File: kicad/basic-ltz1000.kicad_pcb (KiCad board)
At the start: 2 copper layers, 49.5 x 49.5 mm, 43 parts, among them P1 CONN_1X1, P2 CONN_1X1, P3 CONN_1X1, P4 CONN_1X1, P5 CONN_1X1, P6 CONN_2X1, Q1 2N3904, U1 LTZ1000A, U2 LT1013, U30 LTC2057

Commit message: 2.3
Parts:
- added R45: 13k/1k, R_BOX_DIVIDER_PL, F.Cu at (205.1, 93.3)
- moved R4 3.42 mm to (204.5, 96.5)
- moved R5 3.42 mm to (202.6, 98.4)
- moved R2 1.27 mm to (205.1, 71.8)
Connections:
- U30 pad 1: 15V -> (no net)
- U30 pad 8: Vz- Sense -> (no net)
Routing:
- net N-000008: track 26.1 -> 32.7 mm
- net 15V: track 60.1 -> 54.0 mm
- net Vz- Sense: track 245.9 -> 240.1 mm, vias 3 -> 2
- net Vz+ Sense: track 125.0 -> 129.3 mm
- net N-0000023: track 55.3 -> 57.8 mm
- net N-0000014: track 52.9 -> 53.5 mm
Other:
- board text added: "v2.3"
- board text removed: "v2.2b"

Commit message: v2.4 gerbers
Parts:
- removed the G*** at (201.3, 67.7)
- removed P6: CONN_2X1, SIL-2
- added G***: OSHW-logo_silkscreen-front_3mm, OSHW-logo_silkscreen-front_3mm, F.Cu at (200.5, 69.5)
- added H***: Val**, 1pin_032_058, F.Cu at (246.0, 85.9)
- added H***: Val**, 1pin_032_058, F.Cu at (246.0, 91.9)
- added H***: Val**, 1pin_032_058, F.Cu at (199.4, 101.6)
- moved R19 3.14 mm to (213.9, 106.8), turned to 160 degrees
- moved H*** 2.62 mm to (242.6, 71.8)
- moved C30 1.91 mm to (241.9, 80.6)
- moved C31 1.91 mm to (241.9, 83.2)
- moved R31 1.42 mm to (245.7, 77.5)
- moved U30 1.27 mm to (242.6, 88.9)
- moved C33 1.27 mm to (242.6, 94.6)
- moved P1 1.27 mm to (210.8, 111.8)
- moved P4 1.27 mm to (208.3, 111.8)
- moved R2 0.90 mm to (205.7, 72.4)
- moved H1 0.64 mm to (202.6, 109.2)
- moved P2 0.64 mm to (217.8, 69.2)
- moved P3 0.64 mm to (236.2, 92.1)
- moved R32 0.64 mm to (236.2, 79.4)
- moved D3 0.63 mm to (236.9, 111.8)
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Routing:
- net Vz- Sense: track 240.1 -> 220.2 mm
- net (no net): track 0.00 -> 7.94 mm
- net CHASSIS: track 6.54 -> 0.00 mm
- net N-000007: track 14.4 -> 17.1 mm
- net 15V: track 54.0 -> 51.6 mm
- net Vz+ Sense: track 129.3 -> 127.0 mm
- net N-0000023: track 57.8 -> 55.5 mm
- net N-0000012: track 14.2 -> 15.8 mm
- net Vz+ Buf: track 16.2 -> 15.3 mm
- net N-0000014: track 53.5 -> 52.7 mm
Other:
- board size 49.5 x 49.5 mm -> 48.9 x 46.4 mm
- board text added: "+ SD -"
- board text added: "TSET"
- board text added: "v2.4"
- board text removed: "CHASSIS"
- board text removed: "v2.3"

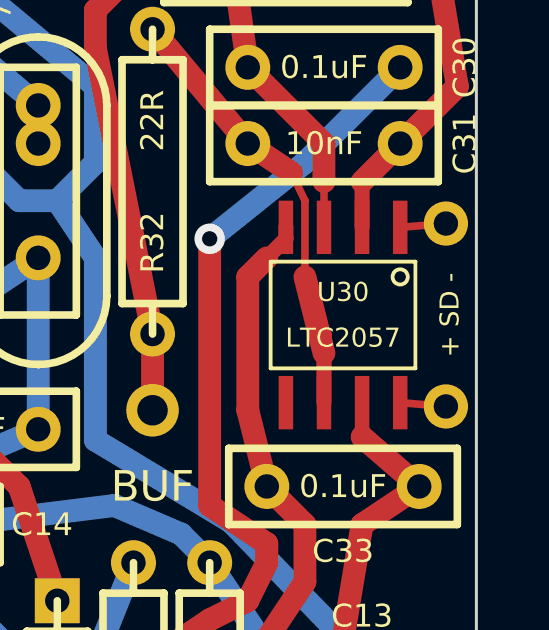
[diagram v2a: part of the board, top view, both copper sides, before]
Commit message: silkscreen typo
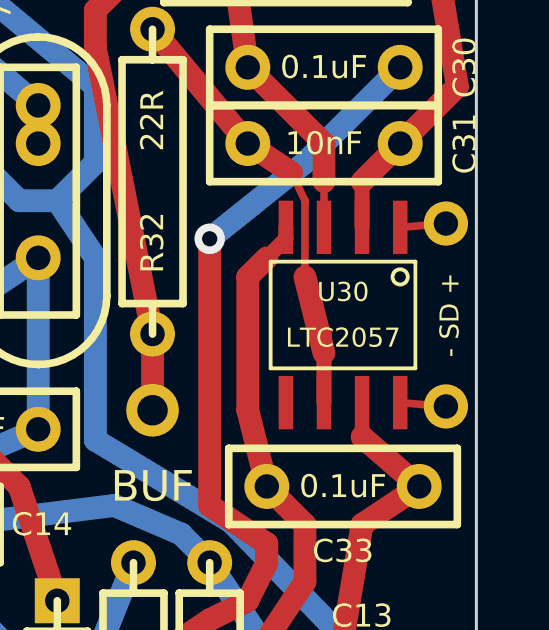
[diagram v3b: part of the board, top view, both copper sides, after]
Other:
- board text added: "- SD +"
- board text removed: "+ SD -"
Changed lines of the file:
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@@
     (links 76)
     (no_connects 0)
-    (area 196.1388 64.388999 248.031001 116.459)
+    (area 196.186778 65.786 249.202222 115.189)
     (thickness 1.6)
     (drawings 21)
@@
     )
   )
-  (gr_text "+ SD -" (at 246.126 88.9 90) (layer F.SilkS)
+  (gr_text "- SD +" (at 246.126 88.9 90) (layer F.SilkS)
     (effects (font (size 0.635 0.635) (thickness 0.127)))
   )

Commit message: v2.4.1
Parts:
- added C32: 0.1uF, BOXCAP_01_03_02_059A, F.Cu at (229.9, 90.2)
- added C9: 0.1uF, BOXCAP_01_03_02_059A, F.Cu at (211.5, 108.6)
- moved D1 8.25 mm to (228.6, 82.5), turned to 270 degrees
- moved R19 3.30 mm to (214.0, 103.5), turned to 180 degrees
- moved R3 2.54 mm to (232.4, 82.5)
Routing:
- net Vz- Sense: track 220.2 -> 240.3 mm
- net N-000005: track 18.6 -> 11.3 mm
- net N-0000023: track 32.3 -> 36.9 mm
- net N-000007: track 8.89 -> 13.4 mm
- net Vz+ Buf: track 15.3 -> 19.6 mm
- net N-000001: track 17.1 -> 19.6 mm
- net Vz+ Sense: track 127.0 -> 127.8 mm
- net H+: track 66.6 -> 67.3 mm
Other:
- board text added: "T SET"
- board text added: "v2.4.1"
- board text removed: "TSET"
- board text removed: "v2.4"

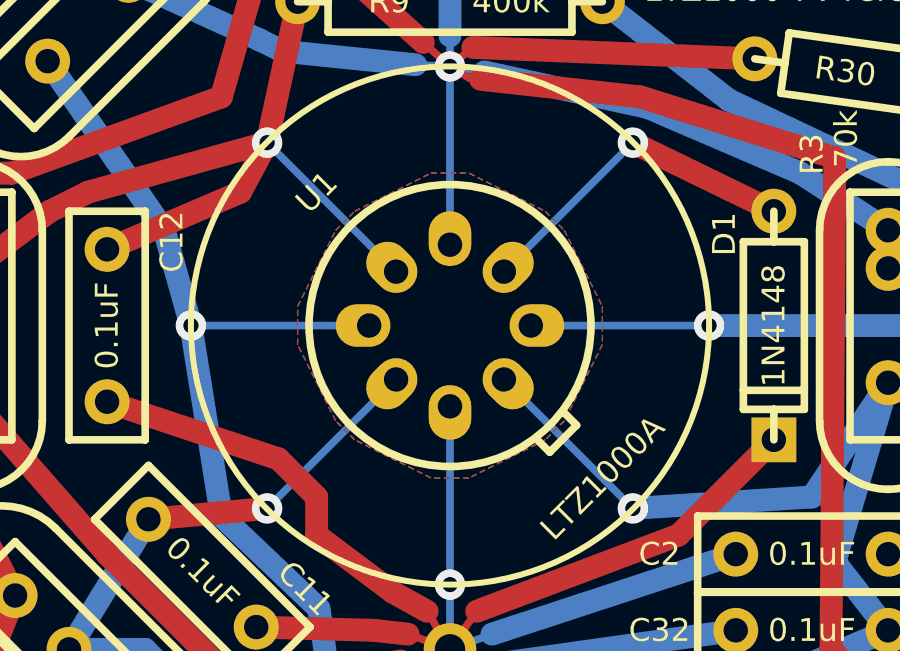
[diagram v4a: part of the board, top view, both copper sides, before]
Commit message: adding vias
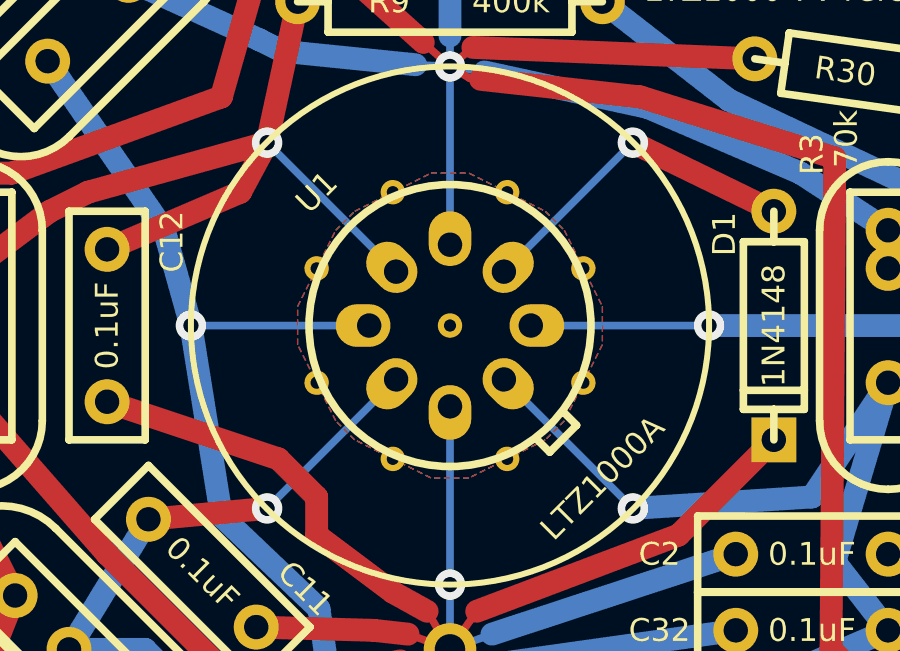
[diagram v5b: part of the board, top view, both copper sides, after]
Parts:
- added H***: Val**, Via_016, F.Cu at (215.9, 87.0)
- added H***: Val**, Via_016, F.Cu at (213.4, 84.5)
- added H***: Val**, Via_016, F.Cu at (213.4, 80.6)
- added H***: Val**, Via_016, F.Cu at (215.9, 78.1)
- added H***: Val**, Via_016, F.Cu at (217.8, 82.5)
- added H***: Val**, Via_016, F.Cu at (219.7, 78.1)
- added H***: Val**, Via_016, F.Cu at (222.2, 80.6)
- added H***: Val**, Via_016, F.Cu at (222.2, 84.5)
- added H***: Val**, Via_016, F.Cu at (219.7, 87.0)
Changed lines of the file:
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@@
     (tracks 267)
     (zones 0)
-    (modules 48)
+    (modules 57)
     (nets 23)
   )
@@
     )
   )
+  (module Via_016 (layer F.Cu)
+    (at 217.805 82.55)
+    (descr "Via, 0.016\"")
+    (path 1pin)
+    (fp_text reference H*** (at 0 -0.635) (layer F.SilkS) hide
+      (effects (font (size 0.127 0.127) (thickness 0.000001)))
+    )
+    (fp_text value Val** (at 0 0.635) (layer F.SilkS) hide
+      (effects (font (size 0.127 0.127) (thickness 0.000001)))
+    )
+    (pad ~ thru_hole oval (at 0 0) (size 0.8128 0.8128) (drill 0.4064)
+      (layers *.Cu)
+      (zone_connect 2)
+    )
+  )
+  (module Via_016 (layer F.Cu)
+    (at 219.71 78.105)
+    (descr "Via, 0.016\"")
+    (path 1pin)
+    (fp_text reference H*** (at 0 -0.635) (layer F.SilkS) hide
+      (effects (font (size 0.127 0.127) (thickness 0.000001)))
+    )
+    (fp_text value Val** (at 0 0.635) (layer F.SilkS) hide
+      (effects (font (size 0.127 0.127) (thickness 0.000001)))
+    )
+    (pad ~ thru_hole oval (at 0 0) (size 0.8128 0.8128) (drill 0.4064)
+      (layers *.Cu)
+      (zone_connect 2)
+    )
+  )
+  (module Via_016 (layer F.Cu)
+    (at 222.25 80.645)
+    (descr "Via, 0.016\"")
+    (path 1pin)
+    (fp_text reference H*** (at 0 -0.635) (layer F.SilkS) hide
+      (effects (font (size 0.127 0.127) (thickness 0.000001)))
+    )
+    (fp_text value Val** (at 0 0.635) (layer F.SilkS) hide
+      (effects (font (size 0.127 0.127) (thickness 0.000001)))
+    )
+    (pad ~ thru_hole oval (at 0 0) (size 0.8128 0.8128) (drill 0.4064)
+      (layers *.Cu)
+      (zone_connect 2)
+    )
+  )
+  (module Via_016 (layer F.Cu)
+    (at 222.25 84.455)
+    (descr "Via, 0.016\"")
+    (path 1pin)
+    (fp_text reference H*** (at 0 -0.635) (layer F.SilkS) hide
+      (effects (font (size 0.127 0.127) (thickness 0.000001)))
+    )
+    (fp_text value Val** (at 0 0.635) (layer F.SilkS) hide
+      (effects (font (size 0.127 0.127) (thickness 0.000001)))
+    )
+    (pad ~ thru_hole oval (at 0 0) (size 0.8128 0.8128) (drill 0.4064)
+      (layers *.Cu)
+      (zone_connect 2)
+    )
+  )
+  (module Via_016 (layer F.Cu)
+    (at 219.71 86.995)
+    (descr "Via, 0.016\"")
+    (path 1pin)
+    (fp_text reference H*** (at 0 -0.635) (layer F.SilkS) hide
+      (effects (font (size 0.127 0.127) (thickness 0.000001)))
+    )
+    (fp_text value Val** (at 0 0.635) (layer F.SilkS) hide
+      (effects (font (size 0.127 0.127) (thickness 0.000001)))
+    )
+    (pad ~ thru_hole oval (at 0 0) (size 0.8128 0.8128) (drill 0.4064)
+      (layers *.Cu)
+      (zone_connect 2)
+    )
+  )
+  (module Via_016 (layer F.Cu)
+    (at 215.9 86.995)
+    (descr "Via, 0.016\"")
+    (path 1pin)
+    (fp_text reference H*** (at 0 -0.635) (layer F.SilkS) hide
+      (effects (font (size 0.127 0.127) (thickness 0.000001)))
+    )
+    (fp_text value Val** (at 0 0.635) (layer F.SilkS) hide
+      (effects (font (size 0.127 0.127) (thickness 0.000001)))
+    )
+    (pad ~ thru_hole oval (at 0 0) (size 0.8128 0.8128) (drill 0.4064)
+      (layers *.Cu)
+      (zone_connect 2)
+    )
+  )
+  (module Via_016 (layer F.Cu)
+    (at 213.36 84.455)
+    (descr "Via, 0.016\"")
+    (path 1pin)
+    (fp_text reference H*** (at 0 -0.635) (layer F.SilkS) hide
+      (effects (font (size 0.127 0.127) (thickness 0.000001)))
+    )
+    (fp_text value Val** (at 0 0.635) (layer F.SilkS) hide
+      (effects (font (size 0.127 0.127) (thickness 0.000001)))
+    )
+    (pad ~ thru_hole oval (at 0 0) (size 0.8128 0.8128) (drill 0.4064)
+      (layers *.Cu)
+      (zone_connect 2)
+    )
+  )
+  (module Via_016 (layer F.Cu)
+    (at 213.36 80.645)
+    (descr "Via, 0.016\"")
+    (path 1pin)
+    (fp_text reference H*** (at 0 -0.635) (layer F.SilkS) hide
+      (effects (font (size 0.127 0.127) (thickness 0.000001)))
+    )
+    (fp_text value Val** (at 0 0.635) (layer F.SilkS) hide
+      (effects (font (size 0.127 0.127) (thickness 0.000001)))
+    )
+    (pad ~ thru_hole oval (at 0 0) (size 0.8128 0.8128) (drill 0.4064)
+      (layers *.Cu)
+      (zone_connect 2)
+    )
+  )
+  (module Via_016 (layer F.Cu)
+    (at 215.9 78.105)
+    (descr "Via, 0.016\"")
+    (path 1pin)
+    (fp_text reference H*** (at 0 -0.635) (layer F.SilkS) hide
+      (effects (font (size 0.127 0.127) (thickness 0.000001)))
+    )
+    (fp_text value Val** (at 0 0.635) (layer F.SilkS) hide
+      (effects (font (size 0.127 0.127) (thickness 0.000001)))
+    )
+    (pad ~ thru_hole oval (at 0 0) (size 0.8128 0.8128) (drill 0.4064)
+      (layers *.Cu)
+      (zone_connect 2)
+    )
+  )

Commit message: v2.4.2
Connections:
- H*** pad ~: (no net) -> CHASSIS (x9)
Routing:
- added copper zone on B.Cu, net CHASSIS
- added copper zone on F.Cu, net CHASSIS
- removed copper zone on B.Cu, net (none)
- removed copper zone on F.Cu, net (none)
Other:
- board text added: "v2.4.2"
- board text removed: "v2.4.1"
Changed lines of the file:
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@@
 (kicad_pcb (version 3) (host pcbnew "(22-Jun-2014 BZR 4027)-stable")
   (general
-    (links 80)
-    (no_connects 0)
+    (links 89)
+    (no_connects 2)
     (area 196.186778 65.786 249.202222 115.189)
     (thickness 1.6)
@@
     (mod_text_size 1 1)
     (mod_text_width 0.15)
-    (pad_size 8.255 8.255)
-    (pad_drill 3.2)
+    (pad_size 0.8128 0.8128)
+    (pad_drill 0.4064)
     (pad_to_mask_clearance 0)
     (aux_axis_origin 0 0)
@@
     (pad ~ thru_hole oval (at 0 0) (size 0.8128 0.8128) (drill 0.4064)
       (layers *.Cu)
+      (net 2 CHASSIS)
       (zone_connect 2)
     )
@@
     (pad ~ thru_hole oval (at 0 0) (size 0.8128 0.8128) (drill 0.4064)
       (layers *.Cu)
+      (net 2 CHASSIS)
       (zone_connect 2)
     )
@@
     (pad ~ thru_hole oval (at 0 0) (size 0.8128 0.8128) (drill 0.4064)
       (layers *.Cu)
+      (net 2 CHASSIS)
       (zone_connect 2)
     )
@@
     (pad ~ thru_hole oval (at 0 0) (size 0.8128 0.8128) (drill 0.4064)
       (layers *.Cu)
+      (net 2 CHASSIS)
       (zone_connect 2)
     )
@@
     (pad ~ thru_hole oval (at 0 0) (size 0.8128 0.8128) (drill 0.4064)
       (layers *.Cu)
+      (net 2 CHASSIS)
       (zone_connect 2)
     )
@@
     (pad ~ thru_hole oval (at 0 0) (size 0.8128 0.8128) (drill 0.4064)
       (layers *.Cu)
+      (net 2 CHASSIS)
       (zone_connect 2)
     )
@@
     (pad ~ thru_hole oval (at 0 0) (size 0.8128 0.8128) (drill 0.4064)
       (layers *.Cu)
+      (net 2 CHASSIS)
       (zone_connect 2)
     )
@@
     (pad ~ thru_hole oval (at 0 0) (size 0.8128 0.8128) (drill 0.4064)
       (layers *.Cu)
+      (net 2 CHASSIS)
       (zone_connect 2)
     )
@@
     (pad ~ thru_hole oval (at 0 0) (size 0.8128 0.8128) (drill 0.4064)
       (layers *.Cu)
+      (net 2 CHASSIS)
       (zone_connect 2)
     )
@@
     (effects (font (size 0.762 0.762) (thickness 0.1524)) (justify left mirror))
   )
-  (gr_text v2.4.1 (at 234.569 69.977) (layer F.SilkS)
+  (gr_text v2.4.2 (at 234.569 69.977) (layer F.SilkS)
     (effects (font (size 0.762 0.762) (thickness 0.1524)) (justify left))
   )
@@
   (segment (start 219.075 99.695) (end 222.25 98.425) (width 0.762) (layer B.Cu) (net 22))
   (segment (start 219.075 99.695) (end 222.25 98.425) (width 0.254) (layer B.Cu) (net 22))
-  (zone (net 0) (net_name "") (layer F.Cu) (hatch edge 0.508)
+  (zone (net 2) (net_name CHASSIS) (layer F.Cu) (hatch edge 0.508)
     (connect_pads (clearance 0.508))
     (min_thickness 0.254)
@@
     (polygon
       (pts
-        (xy 222.885 83.185) (xy 221.615 85.725) (xy 220.98 86.36) (xy 218.44 87.63) (xy 217.17 87.63)
-        (xy 214.63 86.36) (xy 213.995 85.725) (xy 212.725 83.185) (xy 212.725 81.915) (xy 213.995 79.375)
-        (xy 214.63 78.74) (xy 217.17 77.47) (xy 218.44 77.47) (xy 220.98 78.74) (xy 221.615 79.375)
-        (xy 222.885 81.915)
+        (xy 224.155 83.185) (xy 222.885 86.36) (xy 221.615 87.63) (xy 218.44 88.9) (xy 217.17 88.9)
+        (xy 213.995 87.63) (xy 212.725 86.36) (xy 211.455 83.185) (xy 211.455 81.915) (xy 212.725 78.74)
+        (xy 213.995 77.47) (xy 217.17 76.2) (xy 218.44 76.2) (xy 221.615 77.47) (xy 222.885 78.74)
+        (xy 224.155 81.915)
       )
     )
   )
-  (zone (net 0) (net_name "") (layer B.Cu) (hatch edge 0.508)
+  (zone (net 2) (net_name CHASSIS) (layer B.Cu) (hatch edge 0.508)
     (connect_pads (clearance 0.508))
     (min_thickness 0.254)
@@
     (polygon
       (pts
-        (xy 222.885 83.185) (xy 221.615 85.725) (xy 220.98 86.36) (xy 218.44 87.63) (xy 217.17 87.63)
-        (xy 214.63 86.36) (xy 213.995 85.725) (xy 212.725 83.185) (xy 212.725 81.915) (xy 213.995 79.375)
-        (xy 214.63 78.74) (xy 217.17 77.47) (xy 218.44 77.47) (xy 220.98 78.74) (xy 221.615 79.375)
-        (xy 222.885 81.915)
+        (xy 224.155 83.185) (xy 222.885 86.36) (xy 221.615 87.63) (xy 218.44 88.9) (xy 217.17 88.9)
+        (xy 213.995 87.63) (xy 212.725 86.36) (xy 211.455 83.185) (xy 211.455 81.915) (xy 212.725 78.74)
+        (xy 213.995 77.47) (xy 217.17 76.2) (xy 218.44 76.2) (xy 221.615 77.47) (xy 222.885 78.74)
+        (xy 224.155 81.915)
       )
     )
